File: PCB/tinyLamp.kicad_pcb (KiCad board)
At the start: 2 copper layers, 50 x 38 mm, 54 parts, among them J1 USB_B_Mini, J2 Conn_02x03_Odd_Even, Q1 Q_NPN_BCE, Q2 Q_NPN_BCE, Q3 Q_NPN_BCE, Q4 Q_NPN_BCE, SW1 SW_Push, SW2 SW_Push, SW3 SW_Push, SW4 SW_Push, U1 TP4056, U2 ATtiny13A-SS, X1 BATT+, X2 BATT-

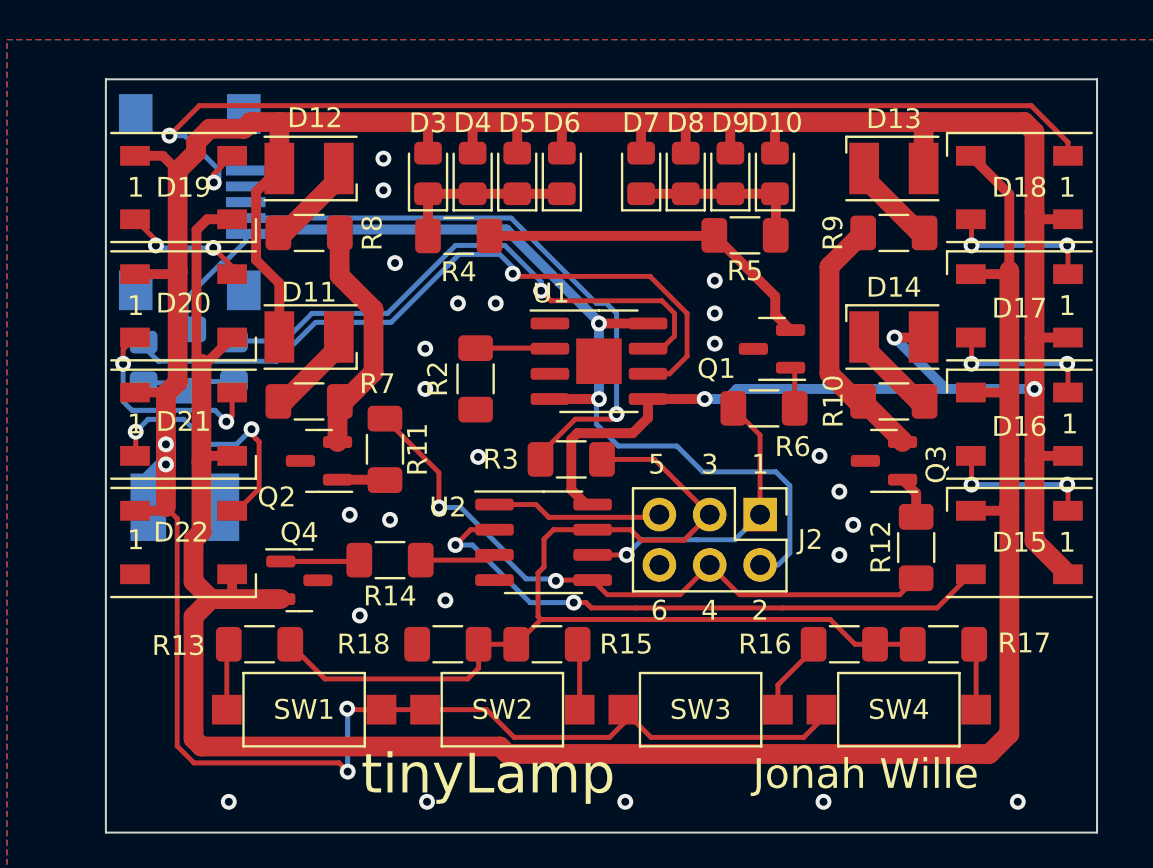
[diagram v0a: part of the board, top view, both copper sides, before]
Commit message: moved usb con inside board parameters
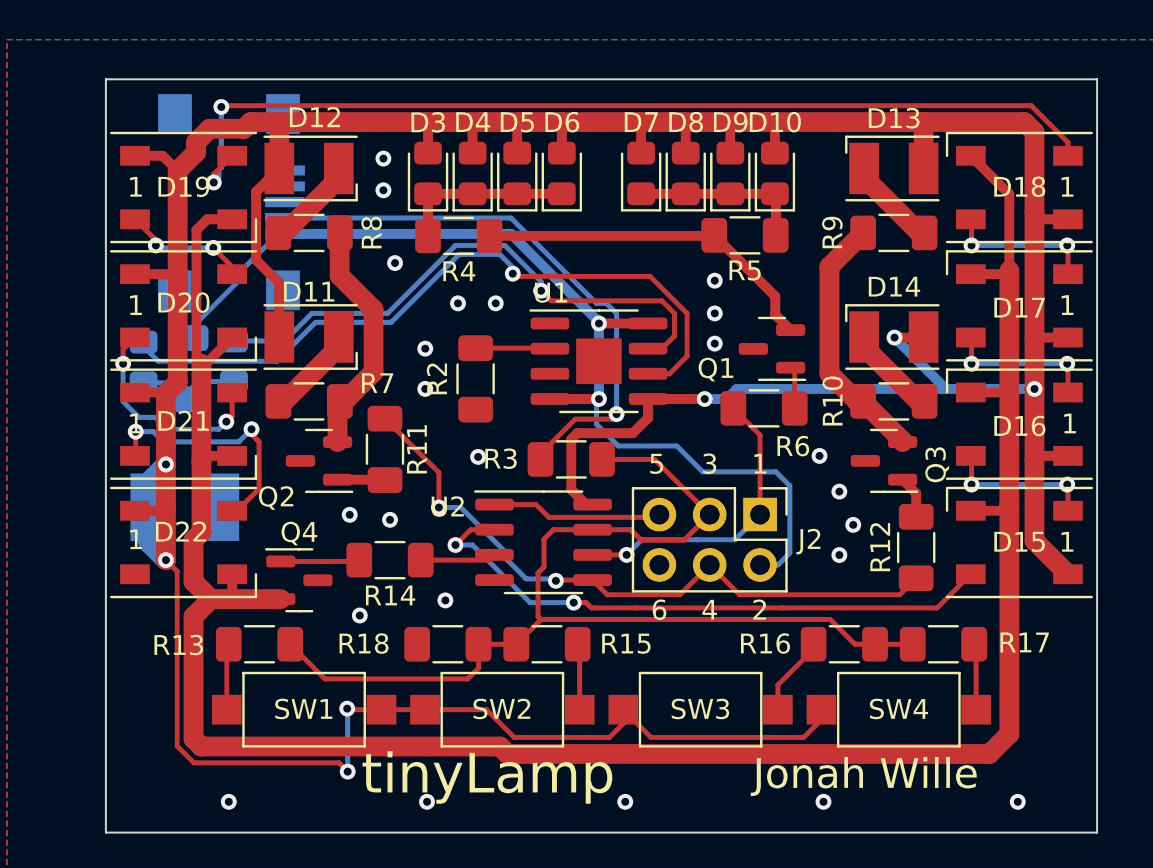
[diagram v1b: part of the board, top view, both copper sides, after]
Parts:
- moved J1 1.97 mm to (-18.7, -1.80)
- moved R1 0.46 mm to (-20.7, 6.60)
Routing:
- net Net-(D18-Pad2): track 53.1 -> 49.9 mm
- net VCC: track 214.7 -> 216.7 mm
- net Net-(J1-Pad2): track 30.7 -> 28.7 mm
- net VBUS: track 52.5 -> 51.4 mm
- net Net-(D21-Pad2): track 13.2 -> 12.5 mm

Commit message: v1
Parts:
- added D1: D, Diode_SMD:D_1206_3216Metric_Pad1.42x1.75mm_HandSolder, F.Cu at (1.52, 0.25)
- added D2: D, Diode_SMD:D_SOD-123, F.Cu at (-23.1, 21.7)
- moved R1 7.05 mm to (5.33, 9.53), turned to -90 degrees
- moved R6 0.82 mm to (9.02, 8.51)
- moved U1 0.63 mm to (-0.13, 6.86)
- moved X1 0.13 mm to (-22.9, 13.5)
- renumbered D9 to D10, D10 to D11, D2 to D12, D11 to D13, D12 to D14, D13 to D15, D14 to D16, D15 to D17, D16 to D18, D17 to D19, D18 to D20, D19 to D21, D20 to D22, D21 to D23, D22 to D24, D1 to D3, D3 to D4, D4 to D5, D5 to D6, D6 to D7, D7 to D8, D8 to D9, R3 to R1, R1 to R2, R2 to R3
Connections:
- J1 pad 3: unconnected-(J1-Pad3) -> /USBIN
- U1 pad 5: VCC -> /BattV
- X1 pad 1: VCC -> /BattV
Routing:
- net /BattV: track 0.00 -> 49.2 mm, vias 0 -> 2
- net /USBIN: track 0.00 -> 22.0 mm, vias 0 -> 1
- net Net-(J1-Pad2): track 28.7 -> 37.0 mm
- net /PB2: track 55.0 -> 51.3 mm
- net Net-(Q1-Pad2): track 17.7 -> 21.1 mm
- net VCC: track 216.7 -> 219.3 mm, vias 7 -> 6
- net /PB0: track 33.3 -> 35.2 mm
- net Net-(D12-Pad1): track 28.6 -> 29.5 mm
- net GND: vias 24 -> 22
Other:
- board text removed: "3"

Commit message: made Sub schematics
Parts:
- removed D1: D, Diode_SMD:D_1206_3216Metric_Pad1.42x1.75mm_HandSolder
- removed D10, D4, D5, D6, D7, D8, D9: LEDA, LED_SMD:LED_0805_2012Metric_Pad1.15x1.40mm_HandSolder
- removed D14, D15, D16: LEDW, LED_SMD:LED_PLCC-2
- removed D17, D18, D19, D20: WS2812B, LED_SMD:LED_WS2812B_PLCC4_5.0x5.0mm_P3.2mm
- removed D2: D, Diode_SMD:D_SOD-123
- removed D3: LEDG, LED_SMD:LED_0805_2012Metric_Pad1.15x1.40mm_HandSolder
- removed J1: USB_B_Mini, Connector_USB:USB_Mini-B_Lumberg_2486_01_Horizontal
- removed J2: Conn_02x03_Odd_Even, Connector_PinHeader_2.54mm:PinHeader_2x03_P2.54mm_Vertical
- removed Q1, Q2, Q3, Q4: Q_NPN_BCE, Package_TO_SOT_SMD:SOT-23
- removed R1, R6: 1k, Resistor_SMD:R_1206_3216Metric_Pad1.30x1.75mm_HandSolder
- removed R10, R7, R8, R9: 15R, Resistor_SMD:R_1206_3216Metric_Pad1.30x1.75mm_HandSolder
- removed R15: 4K7, Resistor_SMD:R_1206_3216Metric_Pad1.30x1.75mm_HandSolder
- removed R16: 2K2, Resistor_SMD:R_1206_3216Metric_Pad1.30x1.75mm_HandSolder
- removed R17: 1K2, Resistor_SMD:R_1206_3216Metric_Pad1.30x1.75mm_HandSolder
- removed R18: 2K7, Resistor_SMD:R_1206_3216Metric_Pad1.30x1.75mm_HandSolder
- removed R2: 1K, Resistor_SMD:R_1206_3216Metric_Pad1.30x1.75mm_HandSolder
- removed R3: 2k, Resistor_SMD:R_1206_3216Metric_Pad1.30x1.75mm_HandSolder
- removed R4, R5: 110R, Resistor_SMD:R_1206_3216Metric_Pad1.30x1.75mm_HandSolder
- removed SW1, SW2, SW3, SW4: SW_Push, Button_Switch_SMD:SW_SPST_CK_RS282G05A3
- removed U1: TP4056, Package_SO:HSOP-8-1EP_3.9x4.9mm_P1.27mm_EP2.3x2.3mm
- removed U2: ATtiny13A-SS, Package_SO:SOIC-8_3.9x4.9mm_P1.27mm
- removed X1: BATT+, TestPoint:TestPoint_Keystone_5015_Micro-Minature
- removed X2: BATT-, TestPoint:TestPoint_Keystone_5015_Micro-Minature
- added D25: LED_RGB, LED_SMD:LED_RGB_5050-6, F.Cu at (21.5, 19.5)
- added D26: LED_RGB, LED_SMD:LED_RGB_5050-6, F.Cu at (21.5, 12.0)
- added D27: LED_RGB, LED_SMD:LED_RGB_5050-6, F.Cu at (21.5, 4.50)
- added D28: LED_RGB, LED_SMD:LED_RGB_5050-6, F.Cu at (21.5, -3.00)
- added D31: LEDA, LED_SMD:LED_0805_2012Metric_Pad1.15x1.40mm_HandSolder, F.Cu at (-6.04, -3.55)
- added D32: LEDA, LED_SMD:LED_0805_2012Metric_Pad1.15x1.40mm_HandSolder, F.Cu at (-3.94, -3.55)
- added D33: LEDA, LED_SMD:LED_0805_2012Metric_Pad1.15x1.40mm_HandSolder, F.Cu at (-1.84, -3.55)
- added D34: LEDA, LED_SMD:LED_0805_2012Metric_Pad1.15x1.40mm_HandSolder, F.Cu at (0.26, -3.55)
- added D35: LEDA, LED_SMD:LED_0805_2012Metric_Pad1.15x1.40mm_HandSolder, F.Cu at (2.36, -3.55)
- added D36: LEDA, LED_SMD:LED_0805_2012Metric_Pad1.15x1.40mm_HandSolder, F.Cu at (4.46, -3.55)
- added D37: LEDA, LED_SMD:LED_0805_2012Metric_Pad1.15x1.40mm_HandSolder, F.Cu at (6.56, -3.55)
- added D38: LEDA, LED_SMD:LED_0805_2012Metric_Pad1.15x1.40mm_HandSolder, F.Cu at (8.66, -3.55)
- added D41: LEDW, LED_SMD:LED_PLCC-2, F.Cu at (-16.8, -4.12)
- added D42: LEDW, LED_SMD:LED_PLCC-2, F.Cu at (-13.0, -4.12)
- added D43: LEDW, LED_SMD:LED_PLCC-2, F.Cu at (12.9, -4.05)
- added D44: LEDW, LED_SMD:LED_PLCC-2, F.Cu at (16.8, -4.05)
- added J11: USB_B_Mini, Connector_USB:USB_Mini-B_Lumberg_2486_01_Horizontal, B.Cu at (-19.0, -2.03)
- added J12: Conn_02x03_Odd_Even, Connector_PinHeader_2.54mm:PinHeader_2x03_P2.54mm_Vertical, F.Cu at (-13.0, 20.2)
- added Q11: Q_PNP_BCE, Package_TO_SOT_SMD:SOT-23, F.Cu at (16.4, 13.4)
- added Q21: Q_NPN_BCE, Package_TO_SOT_SMD:SOT-23, F.Cu at (11.7, 21.1)
- added Q22: Q_NPN_BCE, Package_TO_SOT_SMD:SOT-23, F.Cu at (8.20, 18.8)
- added Q23: Q_NPN_BCE, Package_TO_SOT_SMD:SOT-23, F.Cu at (11.7, 16.3)
- added Q31: Q_PNP_BCE, Package_TO_SOT_SMD:SOT-23, F.Cu at (-9.04, -3.70)
- added Q32: Q_NPN_BCE, Package_TO_SOT_SMD:SOT-23, F.Cu at (7.50, 1.00)
- added Q41: Q_NPN_BCE, Package_TO_SOT_SMD:SOT-23, F.Cu at (11.7, 1.00)
- added R21: 110R, Resistor_SMD:R_1206_3216Metric_Pad1.30x1.75mm_HandSolder, F.Cu at (16.0, 21.9)
- added R22: 1k, Resistor_SMD:R_1206_3216Metric_Pad1.30x1.75mm_HandSolder, F.Cu at (7.40, 22.0)
- added R23: 110R, Resistor_SMD:R_1206_3216Metric_Pad1.30x1.75mm_HandSolder, F.Cu at (16.0, 19.5)
- added R24: 1k, Resistor_SMD:R_1206_3216Metric_Pad1.30x1.75mm_HandSolder, F.Cu at (3.90, 19.6)
- added R25: 110R, Resistor_SMD:R_1206_3216Metric_Pad1.30x1.75mm_HandSolder, F.Cu at (16.0, 17.1)
- added R26: 1k, Resistor_SMD:R_1206_3216Metric_Pad1.30x1.75mm_HandSolder, F.Cu at (7.40, 15.6)
- added R31: 12k, Resistor_SMD:R_1206_3216Metric_Pad1.30x1.75mm_HandSolder, F.Cu at (-2.25, 0.90)
- added R32: 110R, Resistor_SMD:R_1206_3216Metric_Pad1.30x1.75mm_HandSolder, F.Cu at (0.11, 0.90)
- added R33: 110R, Resistor_SMD:R_1206_3216Metric_Pad1.30x1.75mm_HandSolder, F.Cu at (2.46, 0.90)
- added R34: 1k, Resistor_SMD:R_1206_3216Metric_Pad1.30x1.75mm_HandSolder, F.Cu at (7.00, 7.50)
- added R41: 15R, Resistor_SMD:R_1206_3216Metric_Pad1.30x1.75mm_HandSolder, F.Cu at (-16.1, -0.25)
- added R42: 15R, Resistor_SMD:R_1206_3216Metric_Pad1.30x1.75mm_HandSolder, F.Cu at (16.1, -0.15)
- added R43: 1k, Resistor_SMD:R_1206_3216Metric_Pad1.30x1.75mm_HandSolder, F.Cu at (16.1, 2.15)
- added SW11: SW_Push, Button_Switch_SMD:SW_SPST_CK_RS282G05A3, F.Cu at (0.00, 26.0)
- added SW12: SW_Push, Button_Switch_SMD:SW_SPST_CK_RS282G05A3, F.Cu at (-15.0, 26.0)
- added SW13: SW_Push, Button_Switch_SMD:SW_SPST_CK_RS282G05A3, F.Cu at (15.0, 26.0)
- added U11: TP4056, Package_SO:HSOP-8-1EP_3.9x4.9mm_P1.27mm_EP2.3x2.3mm, F.Cu at (-4.60, 7.90)
- added U12: ATtiny24A-SS, Package_SO:SOIC-14_3.9x8.7mm_P1.27mm, F.Cu at (-4.70, 18.8)
- added X11: BATT+, TestPoint:TestPoint_Keystone_5015_Micro-Minature, B.Cu at (-18.9, 12.8)
- added X12: BATT-, TestPoint:TestPoint_Keystone_5015_Micro-Minature, B.Cu at (-19.3, 8.80)
- D11: value LEDA -> D; footprint LED_SMD:LED_0805_2012Metric_Pad1.15x1.40mm_HandSolder -> Diode_SMD:D_SOD-123; moved to B.Cu
- D12: value LEDA -> LEDG; moved to F.Cu
- D13: value LEDW -> LEDA; footprint LED_SMD:LED_PLCC-2 -> LED_SMD:LED_0805_2012Metric_Pad1.15x1.40mm_HandSolder
- D21, D22, D23, D24: value WS2812B -> LED_RGB; footprint LED_SMD:LED_WS2812B_PLCC4_5.0x5.0mm_P3.2mm -> LED_SMD:LED_RGB_5050-6
- R12: value 1k -> 1K
- R13: value 8K2 -> 2k
- R14: value 1k -> 12k
- moved D11 27.6 mm to (-17.5, 5.20), turned to 0 degrees
- moved R14 22.9 mm to (12.0, 13.1), turned to 0 degrees
- moved D21 22.0 mm to (-21.5, 19.5), turned to -90 degrees
- moved D12 20.2 mm to (1.50, 8.40), turned to 0 degrees
- moved D24 18.4 mm to (-21.5, -3.00), turned to -90 degrees
- moved D13 16.3 mm to (1.50, 6.30), turned to 0 degrees
- moved R13 14.9 mm to (-9.70, 7.60), turned to -90 degrees
- moved R12 13.9 mm to (4.60, 7.50)
- moved D22 8.58 mm to (-21.5, 12.0), turned to -90 degrees
- moved R11 7.87 mm to (-12.2, 2.90)
- moved D23 4.92 mm to (-21.5, 4.50), turned to -90 degrees
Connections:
- D11 pad 1: Net-(D10-Pad1) -> /EXTOUT
- D13 pad 2: VCC -> Net-(D12-Pad2)
- D21 pad 1: VCC -> Net-(D21-Pad1)
- D21 pad 4: Net-(D20-Pad2) -> VCC
- D22 pad 1: VCC -> Net-(D21-Pad1)
- D22 pad 2: Net-(D22-Pad2) -> Net-(D21-Pad2)
- D22 pad 4: Net-(D21-Pad2) -> VCC
- D23 pad 1: VCC -> Net-(D21-Pad1)
- D23 pad 2: Net-(D23-Pad2) -> Net-(D21-Pad2)
- D23 pad 4: Net-(D22-Pad2) -> VCC
- D24 pad 1: VCC -> Net-(D21-Pad1)
- D24 pad 2: unconnected-(D24-Pad2) -> Net-(D21-Pad2)
- D24 pad 4: Net-(D23-Pad2) -> VCC
- R11 pad 1: /PB0 -> Net-(J11-Pad2)
- R11 pad 2: Net-(Q2-Pad1) -> /INT3_DATA
- R12 pad 1: /PB0 -> Net-(D12-Pad2)
- R12 pad 2: Net-(Q3-Pad1) -> VBUS
- R13 pad 1: Net-(R13-Pad1) -> /PROG
- R13 pad 2: /PB2 -> GND
- R14 pad 1: /PB4 -> /LEDR_EN
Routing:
- net /RGBleds/LEDR_VCC: track 0.00 -> 126.6 mm
- net Net-(D21-Pad1): track 0.00 -> 121.8 mm, vias 0 -> 8
- net Net-(D21-Pad2): track 6.43 -> 125.6 mm, vias 2 -> 8
- net /PB2: track 51.3 -> 0.00 mm
- net Net-(D20-Pad2): track 49.9 -> 0.00 mm, vias 2 -> 0
- net /BattV: track 49.2 -> 0.00 mm, vias 2 -> 0
- net VCC: track 219.3 -> 170.8 mm, vias 6 -> 4
- net /PWM1: track 0.00 -> 41.5 mm, vias 0 -> 2
- net Net-(J1-Pad2): track 37.0 -> 0.00 mm, vias 1 -> 0
- net Net-(D3-Pad1): track 36.2 -> 0.00 mm, vias 1 -> 0
- net /PWM0: track 0.00 -> 36.2 mm, vias 0 -> 2
- net /INT3_DATA: track 0.00 -> 35.6 mm
- net /PB0: track 35.2 -> 0.00 mm, vias 2 -> 0
- net Net-(Q41-Pad2): track 0.00 -> 31.3 mm
- net /PB3: track 30.3 -> 0.00 mm, vias 2 -> 0
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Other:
- board text added: "3"
- board text removed: "+"
- board text removed: "-"
- board text removed: "JLCJLCJLCJLC"

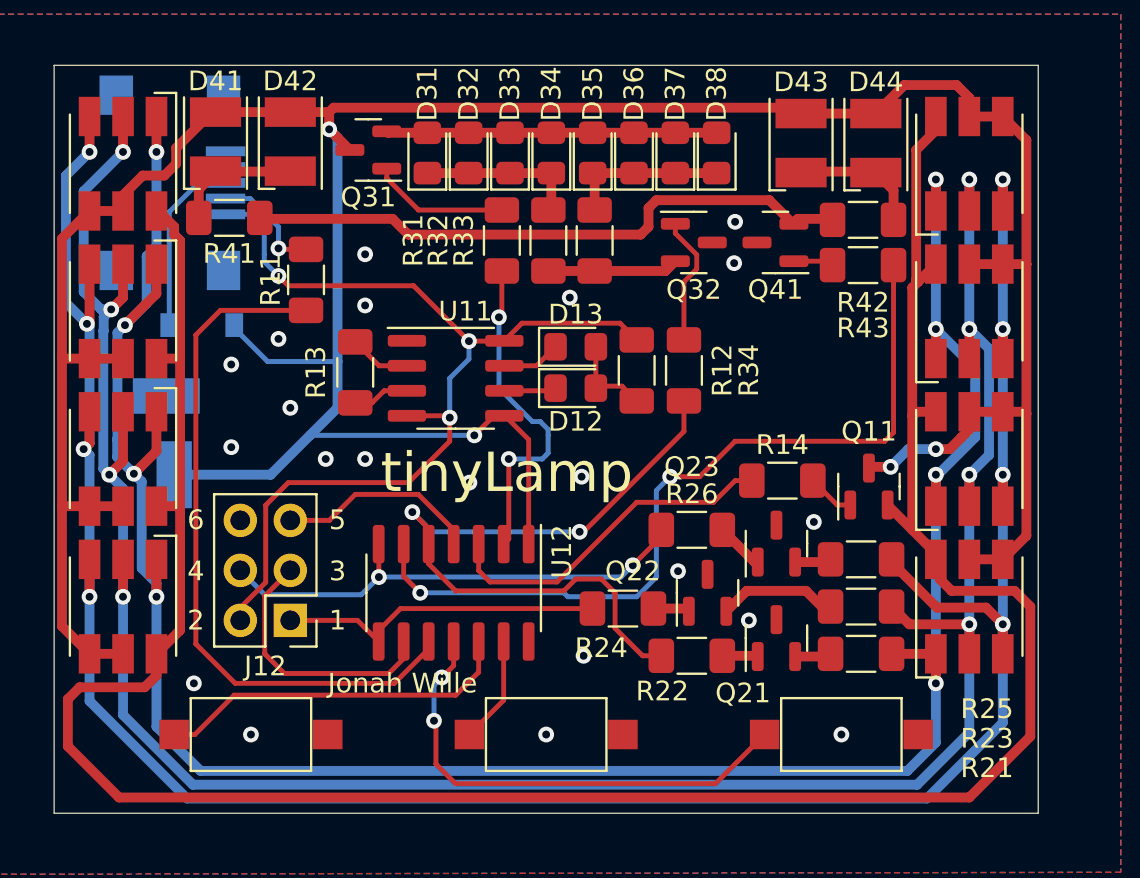
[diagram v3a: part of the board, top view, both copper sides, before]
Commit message: added Capacitor and updated PCB
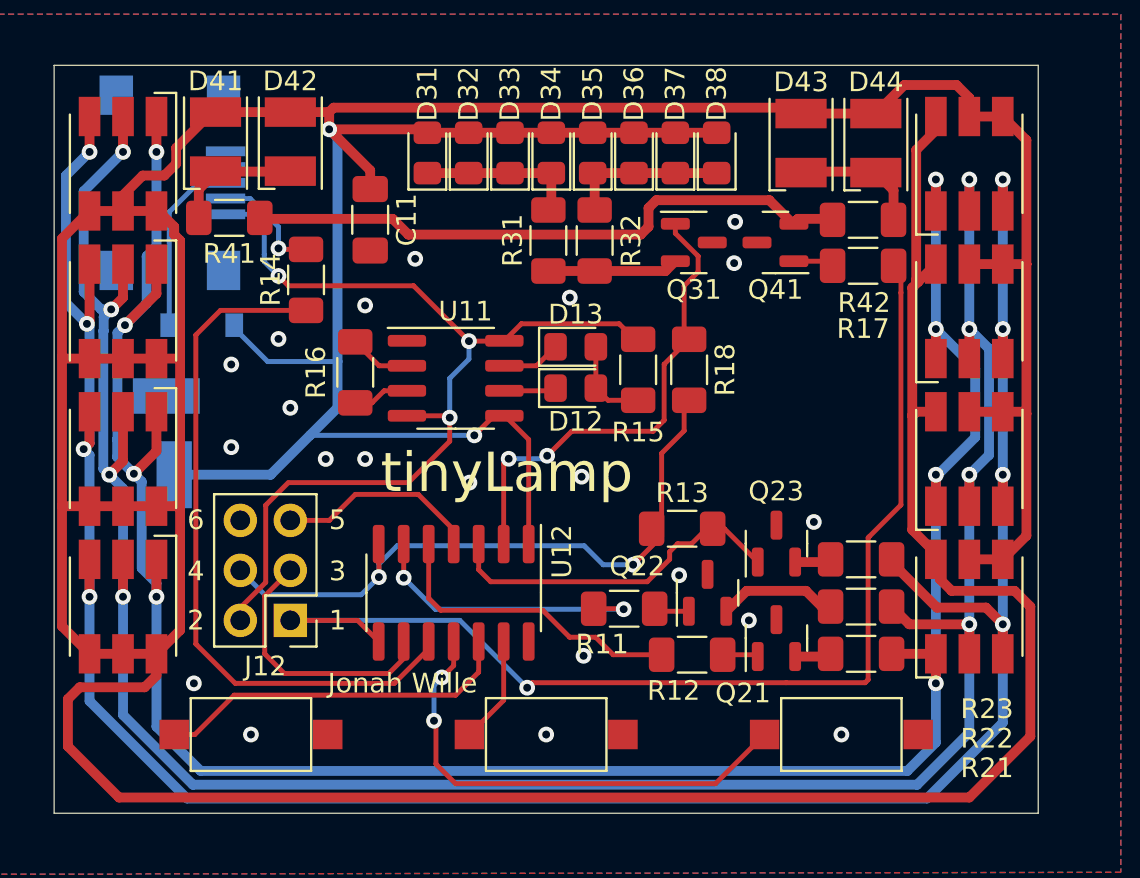
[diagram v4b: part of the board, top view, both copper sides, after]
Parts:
- removed Q11: Q_PNP_BCE, Package_TO_SOT_SMD:SOT-23
- removed the Q31 at (-9.04, -3.70)
- removed the R14 at (12.0, 13.1)
- removed the R22 at (7.40, 22.0)
- removed R24, R26, R34, R43: 1k, Resistor_SMD:R_1206_3216Metric_Pad1.30x1.75mm_HandSolder
- removed the R31 at (-2.25, 0.90)
- added C11: 1nF, Capacitor_SMD:C_1206_3216Metric_Pad1.33x1.80mm_HandSolder, F.Cu at (-8.94, -0.15)
- added R11: 1K, Resistor_SMD:R_1206_3216Metric_Pad1.30x1.75mm_HandSolder, F.Cu at (3.96, 19.6)
- added R13: 1K, Resistor_SMD:R_1206_3216Metric_Pad1.30x1.75mm_HandSolder, F.Cu at (6.91, 15.5)
- added R15: 1k, Resistor_SMD:R_1206_3216Metric_Pad1.30x1.75mm_HandSolder, F.Cu at (4.67, 7.47)
- added R17: 1K, Resistor_SMD:R_1206_3216Metric_Pad1.30x1.75mm_HandSolder, F.Cu at (16.1, 2.18)
- added R18: 1K, Resistor_SMD:R_1206_3216Metric_Pad1.30x1.75mm_HandSolder, F.Cu at (7.26, 7.47)
- moved R12 14.7 mm to (7.42, 21.9), turned to 0 degrees
- renumbered Q32 to Q31, R11 to R14, R13 to R16, R23 to R22, R25 to R23, R32 to R31, R33 to R32
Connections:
- D21 pad 6: /RGBleds/LEDR_VCC -> VCC
- D22 pad 6: /RGBleds/LEDR_VCC -> VCC
- D23 pad 6: /RGBleds/LEDR_VCC -> VCC
- D24 pad 6: /RGBleds/LEDR_VCC -> VCC
- D25 pad 6: /RGBleds/LEDR_VCC -> VCC
- D26 pad 6: /RGBleds/LEDR_VCC -> VCC
- D27 pad 6: /RGBleds/LEDR_VCC -> VCC
- D28 pad 6: /RGBleds/LEDR_VCC -> VCC
- D31 pad 2: Net-(D31-Pad2) -> VCC
- D32 pad 2: Net-(D31-Pad2) -> VCC
- D33 pad 2: Net-(D31-Pad2) -> VCC
- D34 pad 2: Net-(D31-Pad2) -> VCC
- D35 pad 2: Net-(D31-Pad2) -> VCC
- D36 pad 2: Net-(D31-Pad2) -> VCC
- D37 pad 2: Net-(D31-Pad2) -> VCC
- D38 pad 2: Net-(D31-Pad2) -> VCC
- Q21 pad 1: Net-(Q21-Pad1) -> /RGBleds/LEDR
- Q22 pad 1: Net-(Q22-Pad1) -> /RGBleds/LEDG
- Q23 pad 1: Net-(Q23-Pad1) -> /LEDR_EN
- Q31 pad 1: Net-(Q32-Pad1) -> /LEDA_EN
- Q41 pad 1: Net-(Q41-Pad1) -> /ledW/LEDW
- R12 pad 1: Net-(D12-Pad2) -> /PWM0
- R12 pad 2: VBUS -> /RGBleds/LEDR
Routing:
- net VCC: track 170.8 -> 317.8 mm, vias 4 -> 2
- net /RGBleds/LEDR_VCC: track 126.6 -> 0.00 mm
- net /MISO_PWM3: track 16.8 -> 57.8 mm, vias 0 -> 1
- net /PWM1: track 41.5 -> 15.1 mm
- net /PWM0: track 36.2 -> 15.8 mm, vias 2 -> 0
- net Net-(D31-Pad2): track 16.8 -> 0.00 mm
- net /MOSI_PWM2: track 25.2 -> 33.4 mm
- net /LEDA_EN: track 17.1 -> 24.4 mm
- net Net-(Q31-Pad1): track 7.01 -> 0.00 mm
- net Net-(Q32-Pad1): track 6.62 -> 0.00 mm
- net Net-(Q23-Pad1): track 2.48 -> 0.00 mm
- net Net-(Q11-Pad1): track 2.41 -> 0.00 mm
- net Net-(Q41-Pad1): track 2.07 -> 0.00 mm
- net /ledW/LEDW: track 0.00 -> 2.07 mm
- net Net-(Q22-Pad1): track 1.86 -> 0.00 mm
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
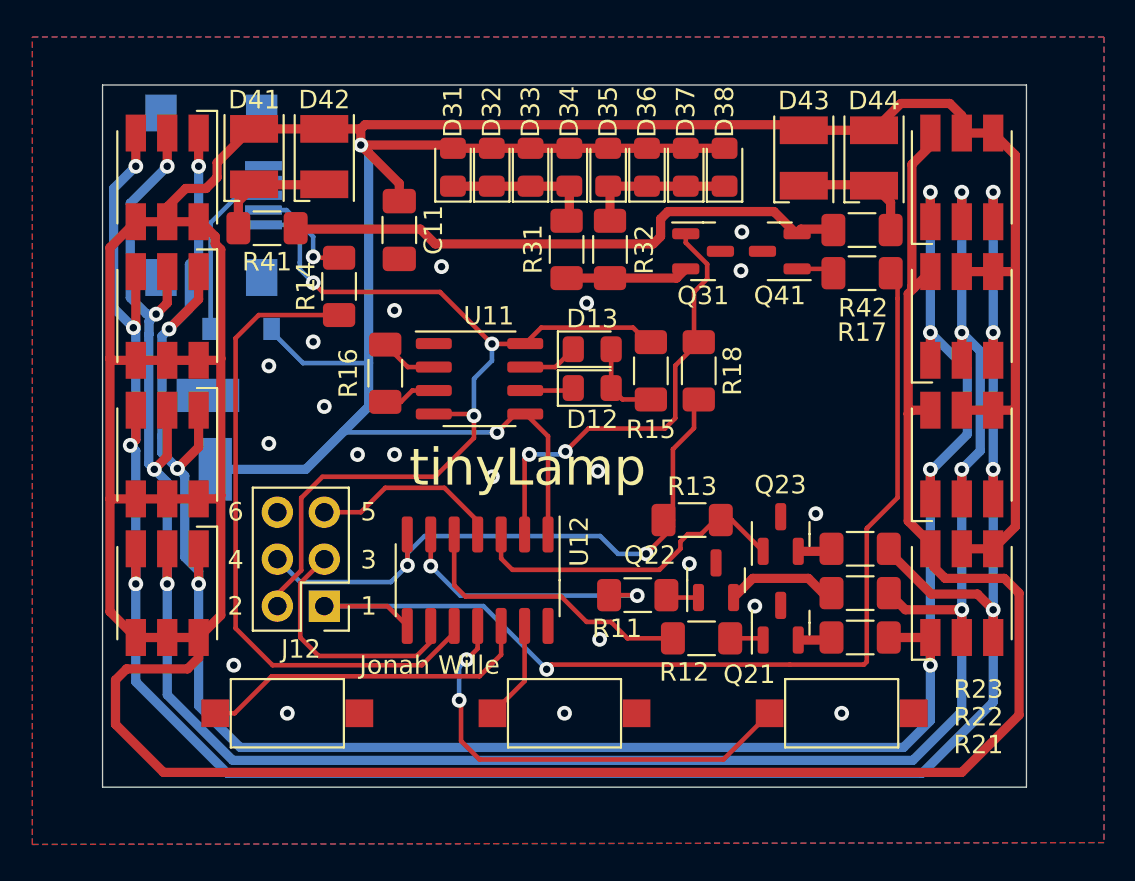
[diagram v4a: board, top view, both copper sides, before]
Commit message: made some changes on RGB LEDs
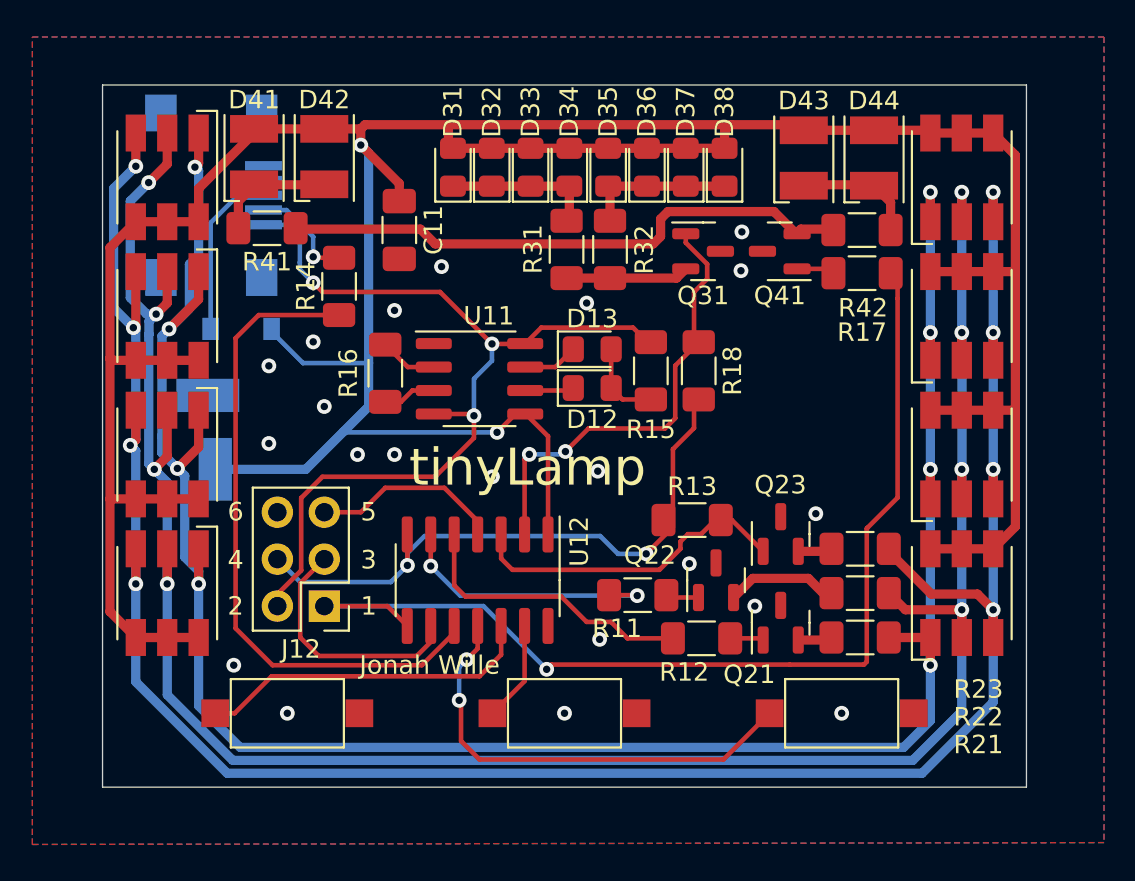
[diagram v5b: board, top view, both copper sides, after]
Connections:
- net Net-(D21-Pad1) renamed /RGBleds/Rch
- net Net-(D21-Pad2) renamed /RGBleds/Gch
- net Net-(D21-Pad3) renamed /RGBleds/Bch
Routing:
- net VCC: track 317.8 -> 192.5 mm
- net /RGBleds/Rch: track 121.8 -> 120.3 mm
- net /RGBleds/Gch: track 125.6 -> 124.8 mm
